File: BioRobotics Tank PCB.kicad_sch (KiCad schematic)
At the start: 35 parts, among them J1 Conn_01x02, J8 Conn_02x05_Odd_Even, J9 Conn_01x05, Q1 IPD060N03LGATMA1, U1 rp2040-zero, U6 TCA9554DB, U7 TCA9554DB, U8 LTC4357MS8, U9 INA219BIDR

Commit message: Add 10k pulldown to nSleep and export BOM
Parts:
- added R15: 10k, Resistor_SMD:R_0805_2012Metric_Pad1.20x1.40mm_HandSolder, symbol Device:R
- C3: Mfr. No (none) -> UVZ1J101MPD
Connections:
- net GND1: now also R15.2
- net ~{M_SLEEP}: now also R15.1
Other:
- note added: "Pulldown"
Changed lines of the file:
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@@
+    (stroke (width 0) (type default))
+  )
+  (wire (pts (xy 87.63 100.33) (xy 90.17 100.33))
     (stroke (width 0) (type default))
   )
@@
     (stroke (width 0) (type default))
   )
+  (wire (pts (xy 77.47 100.33) (xy 80.01 100.33))
+    (stroke (width 0) (type default))
+  )
   (wire (pts (xy 45.72 71.12) (xy 44.45 71.12))
     (stroke (width 0) (type default))
@@
     (stroke (width 0) (type default))
   )
+  (wire (pts (xy 90.17 101.6) (xy 90.17 100.33))
+    (stroke (width 0) (type default))
+  )
   (wire (pts (xy 149.86 86.36) (xy 151.13 86.36))
     (stroke (width 0) (type default))
@@
   )
   (rectangle (start 97.79 16.51) (end 160.02 71.12)
+    (stroke (width 0) (type default))
+    (fill (type none))
+  )
+  (rectangle (start 66.04 87.63) (end 95.25 110.49)
     (stroke (width 0) (type default))
     (fill (type none))
@@
     (effects (font (size 2.54 2.54) (thickness 0.508) bold) (justify left bottom))
   )
+  (text "Pulldown" (at 71.12 92.71 0)
+    (effects (font (size 2.54 2.54) (thickness 0.508) bold) (justify left bottom))
+  )
   (text "3.3V Regulator" (at 38.1 21.59 0)
     (effects (font (size 2.54 2.54) (thickness 0.508) bold) (justify left bottom))
@@
   )
   (label "GPIO11" (at 107.95 96.52 180) (fields_autoplaced)
+    (effects (font (size 1.27 1.27)) (justify right bottom))
+  )
+  (label "~{M_SLEEP}" (at 77.47 100.33 180) (fields_autoplaced)
     (effects (font (size 1.27 1.27)) (justify right bottom))
   )
@@
     )
   )
+  (symbol (lib_id "power:GND1") (at 90.17 101.6 0) (unit 1)
+    (in_bom yes) (on_board yes) (dnp no) (fields_autoplaced)
+    (property "Reference" "#PWR024" (at 90.17 107.95 0)
+      (effects (font (size 1.27 1.27)) hide)
+    )
+    (property "Value" "GND1" (at 90.17 106.68 0)
+      (effects (font (size 1.27 1.27)))
+    )
+    (property "Footprint" "" (at 90.17 101.6 0)
+      (effects (font (size 1.27 1.27)) hide)
+    )
+    (property "Datasheet" "" (at 90.17 101.6 0)
+      (effects (font (size 1.27 1.27)) hide)
+    )
+    (pin "1")
+    (instances
+      (project "BioRobotics Tank PCB"
+        (path "/738c766b-5149-4d22-8944-003aead1c6f2/91fbf09a-497d-4de7-ab4a-2985c5e3b4aa"
+          (reference "#PWR024") (unit 1)
+        )
+        (path "/738c766b-5149-4d22-8944-003aead1c6f2/a65e5353-4be6-414a-8225-04b1dd46f16e"
+          (reference "#PWR032") (unit 1)
+        )
+        (path "/738c766b-5149-4d22-8944-003aead1c6f2/917f7088-b2e9-4770-ad29-156eaf4e2242"
+          (reference "#PWR034") (unit 1)
+        )
+        (path "/738c766b-5149-4d22-8944-003aead1c6f2/05b32763-3ed9-4afa-8241-412ea6f0290d"
+          (reference "#PWR035") (unit 1)
+        )
+        (path "/738c766b-5149-4d22-8944-003aead1c6f2"
+          (reference "#PWR062") (unit 1)
+        )
+      )
+    )
+  )
   (symbol (lib_id "power:+3V3") (at 130.81 86.36 0) (unit 1)
     (in_bom yes) (on_board yes) (dnp no) (fields_autoplaced)
@@
     )
     (property "Datasheet" "~" (at 77.47 35.56 0)
+      (effects (font (size 1.27 1.27)) hide)
+    )
+    (property "Mfr. No" "UVZ1J101MPD" (at 77.47 35.56 0)
       (effects (font (size 1.27 1.27)) hide)
     )
@@
         )
       )
+    )
+  )
+  (symbol (lib_id "Device:R") (at 83.82 100.33 90) (unit 1)
+    (in_bom yes) (on_board yes) (dnp no) (fields_autoplaced)
+    (property "Reference" "R15" (at 83.82 95.25 90)
+      (effects (font (size 1.27 1.27)))
+    )
+    (property "Value" "10k" (at 83.82 97.79 90)
+      (effects (font (size 1.27 1.27)))
+    )
+    (property "Footprint" "Resistor_SMD:R_0805_2012Metric_Pad1.20x1.40mm_HandSolder" (at 83.82 102.108 90)
+      (effects (font (size 1.27 1.27)) hide)
+    )
+    (property "Datasheet" "~" (at 83.82 100.33 0)
+      (effects (font (size 1.27 1.27)) hide)
+    )
+    (property "Mfr. No" "CRS0805-FX-1002ELF" (at 83.82 100.33 90)
+      (effects (font (size 1.27 1.27)) hide)
+    )
+    (pin "1")
+    (pin "2")
+    (instances
+      (project "BioRobotics Tank PCB"
+        (path "/738c766b-5149-4d22-8944-003aead1c6f2"
+          (reference "R15") (unit 1)
+        )
+      )

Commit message: Update 0.1uF capacitor mfr no
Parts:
- C1: Mfr. No KGM21NR71E104KT -> 08055C104JAT2A
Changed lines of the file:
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@@
       (effects (font (size 1.27 1.27)) hide)
     )
-    (property "Mfr. No" "KGM21NR71E104KT" (at 26.67 39.37 90)
+    (property "Mfr. No" "08055C104JAT2A" (at 26.67 39.37 90)
       (effects (font (size 1.27 1.27)) hide)
     )
@@
       (effects (font (size 1.27 1.27)) hide)
     )
-    (property "Mfr. No" "KGM21NR71E104KT" (at 30.48 143.51 90)
+    (property "Mfr. No" "08055C104JAT2A" (at 30.48 143.51 90)
       (effects (font (size 1.27 1.27)) hide)
     )
@@
       (effects (font (size 1.27 1.27)) hide)
     )
-    (property "Mfr. No" "KGM21NR71E104KT" (at 53.34 95.25 90)
+    (property "Mfr. No" "08055C104JAT2A" (at 53.34 95.25 90)
       (effects (font (size 1.27 1.27)) hide)
     )
@@
       (effects (font (size 1.27 1.27)) hide)
     )
-    (property "Mfr. No" "KGM21NR71E104KT" (at 256.54 135.89 90)
+    (property "Mfr. No" "08055C104JAT2A" (at 256.54 135.89 90)
       (effects (font (size 1.27 1.27)) hide)
     )
@@
       (effects (font (size 1.27 1.27)) hide)
     )
-    (property "Mfr. No" "KGM21NR71E104KT" (at 93.98 140.97 90)
+    (property "Mfr. No" "08055C104JAT2A" (at 93.98 140.97 90)
       (effects (font (size 1.27 1.27)) hide)
     )
@@
       (effects (font (size 1.27 1.27)) hide)
     )
-    (property "Mfr. No" "KGM21NR71E104KT" (at 203.2 134.62 90)
+    (property "Mfr. No" "08055C104JAT2A" (at 203.2 134.62 90)
       (effects (font (size 1.27 1.27)) hide)
     )
@@
       (effects (font (size 1.27 1.27)) hide)
     )
-    (property "Mfr. No" "KGM21NR71E104KT" (at 82.55 35.56 90)
+    (property "Mfr. No" "08055C104JAT2A" (at 82.55 35.56 90)
       (effects (font (size 1.27 1.27)) hide)
     )
@@
       (effects (font (size 1.27 1.27)) hide)
     )
-    (property "Mfr. No" "KGM21NR71E104KT" (at 147.32 58.42 90)
-      (effects (font (size 1.27 1.27)) hide)
-    )
+    (property "Mfr. No" "08055C104JAT2A" (at 147.32 58.42 90)
+      (effects (font (size 1.27 1.27)) hide)
+    )

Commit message: Change Screw Terminal Part and update Mfr No's
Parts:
- J1: footprint TerminalBlock_Phoenix:TerminalBlock_Phoenix_MKDS-1,5-2-5.08_1x02_P5.08mm_Horizontal -> TB009-508-02BE:CUI_TB009-508-02BE; Mfr. No (none) -> TB009-508-02BE
- J8: Mfr. No (none) -> 61201021621
- PS1: Mfr. No (none) -> P78E03-1000
- Q1: Mfr. No (none) -> IPD060N03LGATMA1
- U8: Mfr. No (none) -> LTC4357CMS8#PBF
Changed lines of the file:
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@@
       (effects (font (size 1.27 1.27)) (justify left))
     )
-    (property "Footprint" "TerminalBlock_Phoenix:TerminalBlock_Phoenix_MKDS-1,5-2-5.08_1x02_P5.08mm_Horizontal" (at 123.19 127 0)
+    (property "Footprint" "TB009-508-02BE:CUI_TB009-508-02BE" (at 123.19 127 0)
       (effects (font (size 1.27 1.27)) hide)
     )
     (property "Datasheet" "~" (at 123.19 127 0)
+      (effects (font (size 1.27 1.27)) hide)
+    )
+    (property "Mfr. No" "TB009-508-02BE" (at 123.19 127 0)
       (effects (font (size 1.27 1.27)) hide)
     )
@@
       (effects (font (size 1.27 1.27)) (justify left bottom) hide)
     )
+    (property "Mfr. No" "P78E03-1000" (at 49.53 35.56 0)
+      (effects (font (size 1.27 1.27)) hide)
+    )
     (pin "1")
     (pin "2")
@@
     (property "Arrow Price/Stock" "https://www.arrow.com/en/products/ipd060n03lgatma1/infineon-technologies-ag?region=nac" (at -964.44 67.31 0)
       (effects (font (size 1.27 1.27)) (justify left top) hide)
+    )
+    (property "Mfr. No" "IPD060N03LGATMA1" (at 34.29 78.74 90)
+      (effects (font (size 1.27 1.27)) hide)
     )
     (pin "1")
@@
       (effects (font (size 1.27 1.27)) hide)
     )
+    (property "Mfr. No" "61201021621" (at 116.84 93.98 0)
+      (effects (font (size 1.27 1.27)) hide)
+    )
     (pin "1")
     (pin "10")
@@
       (effects (font (size 1.27 1.27)) hide)
     )
+    (property "Mfr. No" "LTC4357CMS8#PBF" (at 43.18 88.9 0)
+      (effects (font (size 1.27 1.27)) hide)
+    )
     (pin "1")
     (pin "2")
@@
       (effects (font (size 1.27 1.27)) (justify left))
     )
-    (property "Footprint" "TerminalBlock_Phoenix:TerminalBlock_Phoenix_MKDS-1,5-2-5.08_1x02_P5.08mm_Horizontal" (at 123.19 139.7 0)
+    (property "Footprint" "TB009-508-02BE:CUI_TB009-508-02BE" (at 123.19 139.7 0)
       (effects (font (size 1.27 1.27)) hide)
     )
     (property "Datasheet" "~" (at 123.19 139.7 0)
+      (effects (font (size 1.27 1.27)) hide)
+    )
+    (property "Mfr. No" "TB009-508-02BE" (at 123.19 139.7 0)
       (effects (font (size 1.27 1.27)) hide)
     )
@@
       (effects (font (size 1.27 1.27)) (justify left))
     )
-    (property "Footprint" "TerminalBlock_Phoenix:TerminalBlock_Phoenix_MKDS-1,5-2-5.08_1x02_P5.08mm_Horizontal" (at 123.19 133.35 0)
+    (property "Footprint" "TB009-508-02BE:CUI_TB009-508-02BE" (at 123.19 133.35 0)
       (effects (font (size 1.27 1.27)) hide)
     )
@@
       (effects (font (size 1.27 1.27)) hide)
     )
+    (property "Mfr. No" "TB009-508-02BE" (at 123.19 133.35 0)
+      (effects (font (size 1.27 1.27)) hide)
+    )

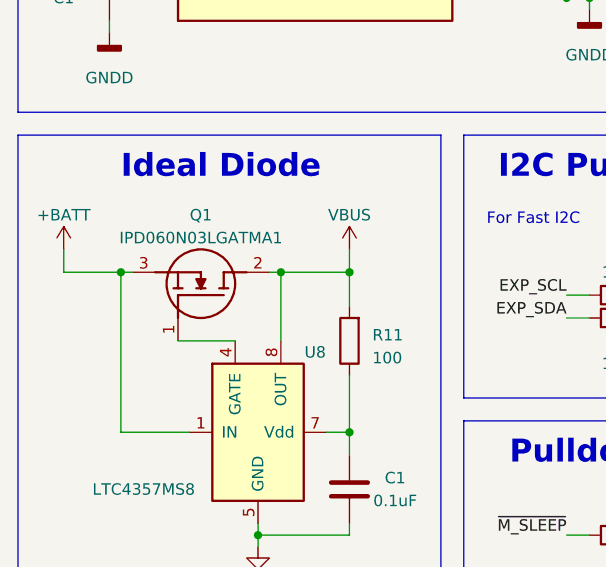
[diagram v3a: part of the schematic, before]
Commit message: Change ideal diode mosfet and increase track sizes
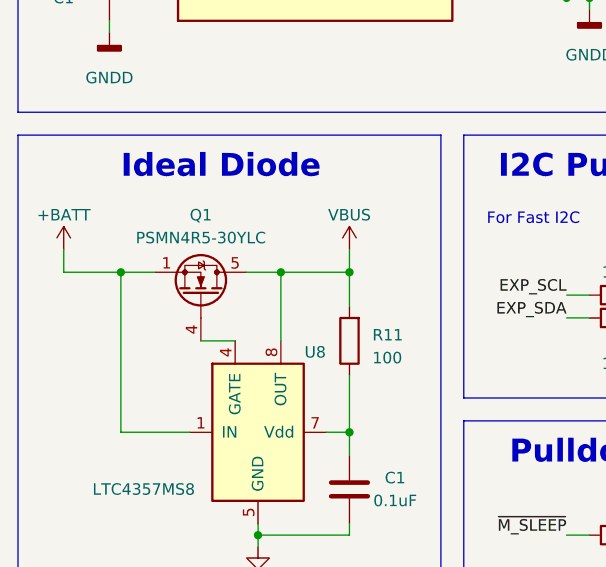
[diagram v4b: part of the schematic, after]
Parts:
- removed Q1: IPD060N03LGATMA1, IPD060N03LGATMA1:IPD060N03LGATMA1, symbol IPD060N03LGATMA1:IPD060N03LGATMA1
- added Q1: PSMN4R5-30YLC, Package_TO_SOT_SMD:LFPAK56, symbol Transistor_FET:PSMN5R2-60YL
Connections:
- net +BATT: now also Q1.1 (S), Q1.2 (S), Q1.3 (S)
- net VBUS: now also Q1.5 (D)
- net at U8.4 (GATE): now also Q1.4 (G)
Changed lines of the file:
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@@
-    (stroke (width 0) (type default))
-  )
-  (wire (pts (xy 34.29 78.74) (xy 40.64 78.74))
     (stroke (width 0) (type default))
   )
@@
     (stroke (width 0) (type default))
   )
-  (wire (pts (xy 27.94 71.12) (xy 29.21 71.12))
+  (wire (pts (xy 27.94 71.12) (xy 31.75 71.12))
     (stroke (width 0) (type default))
   )
@@
     (stroke (width 0) (type default))
   )
-  (wire (pts (xy 45.72 71.12) (xy 44.45 71.12))
+  (wire (pts (xy 41.91 71.12) (xy 45.72 71.12))
     (stroke (width 0) (type default))
   )
@@
   )
   (wire (pts (xy 82.55 31.75) (xy 82.55 30.48))
+    (stroke (width 0) (type default))
+  )
+  (wire (pts (xy 36.83 78.74) (xy 40.64 78.74))
     (stroke (width 0) (type default))
   )
@@
         (path "/738c766b-5149-4d22-8944-003aead1c6f2"
           (reference "JP2") (unit 1)
-        )
-      )
-    )
-  )
-  (symbol (lib_id "IPD060N03LGATMA1:IPD060N03LGATMA1") (at 34.29 78.74 270) (mirror x) (unit 1)
-    (in_bom yes) (on_board yes) (dnp no)
-    (property "Reference" "Q1" (at 36.83 64.77 90)
-      (effects (font (size 1.27 1.27)))
-    )
-    (property "Value" "IPD060N03LGATMA1" (at 36.83 67.31 90)
-      (effects (font (size 1.27 1.27)))
-    )
-    (property "Footprint" "IPD060N03LGATMA1:IPD060N03LGATMA1" (at -64.44 67.31 0)
-      (effects (font (size 1.27 1.27)) (justify left top) hide)
-    )
-    (property "Datasheet" "https://www.infineon.com/dgdl/Infineon-IPD060N03L%20G-DataSheet-v02_02-EN.pdf?fileId=db3a30432313ff5e01239e4d33a3702f" (at -164.44 67.31 0)
-      (effects (font (size 1.27 1.27)) (justify left top) hide)
-    )
-    (property "Height" "2.5" (at -364.44 67.31 0)
-      (effects (font (size 1.27 1.27)) (justify left top) hide)
-    )
-    (property "Manufacturer_Name" "Infineon" (at -464.44 67.31 0)
-      (effects (font (size 1.27 1.27)) (justify left top) hide)
-    )
-    (property "Manufacturer_Part_Number" "IPD060N03LGATMA1" (at -564.44 67.31 0)
-      (effects (font (size 1.27 1.27)) (justify left top) hide)
-    )
-    (property "Mouser Part Number" "726-IPD060N03LGATMA1" (at -664.44 67.31 0)
-      (effects (font (size 1.27 1.27)) (justify left top) hide)
-    )
-    (property "Mouser Price/Stock" "https://www.mouser.co.uk/ProductDetail/Infineon-Technologies/IPD060N03LGATMA1?qs=Dj8dEyEphkPMHEbgPBJgAQ%3D%3D" (at -764.44 67.31 0)
-      (effects (font (size 1.27 1.27)) (justify left top) hide)
-    )
-    (property "Arrow Part Number" "IPD060N03LGATMA1" (at -864.44 67.31 0)
-      (effects (font (size 1.27 1.27)) (justify left top) hide)
-    )
-    (property "Arrow Price/Stock" "https://www.arrow.com/en/products/ipd060n03lgatma1/infineon-technologies-ag?region=nac" (at -964.44 67.31 0)
-      (effects (font (size 1.27 1.27)) (justify left top) hide)
-    )
-    (property "Mfr. No" "IPD060N03LGATMA1" (at 34.29 78.74 90)
-      (effects (font (size 1.27 1.27)) hide)
-    )
-    (pin "1")
-    (pin "2")
-    (pin "3")
-    (instances
-      (project "BioRobotics Tank PCB"
-        (path "/738c766b-5149-4d22-8944-003aead1c6f2"
-          (reference "Q1") (unit 1)
         )
       )
@@
         )
       )
+    )
+  )
+  (symbol (lib_id "Transistor_FET:PSMN5R2-60YL") (at 36.83 73.66 270) (mirror x) (unit 1)
+    (in_bom yes) (on_board yes) (dnp no)
+    (property "Reference" "Q1" (at 36.83 64.77 90)
+      (effects (font (size 1.27 1.27)))
+    )
+    (property "Value" "PSMN4R5-30YLC" (at 36.83 67.31 90)
+      (effects (font (size 1.27 1.27)))
+    )
+    (property "Footprint" "Package_TO_SOT_SMD:LFPAK56" (at 36.83 69.85 0)
+      (effects (font (size 1.27 1.27)) hide)
+    )
+    (property "Datasheet" "https://www.mouser.co.uk/datasheet/2/916/PSMN4R5_30YLC-2938954.pdf" (at 36.83 73.66 0)
+      (effects (font (size 1.27 1.27)) hide)
+    )
+    (property "Mfr. No" "PSMN4R5-30YLC,115" (at 36.83 73.66 90)
+      (effects (font (size 1.27 1.27)) hide)
+    )
+    (pin "1")
+    (pin "2")
+    (pin "3")
+    (pin "4")
+    (pin "5")
+    (instances
+      (project "BioRobotics Tank PCB"
+        (path "/738c766b-5149-4d22-8944-003aead1c6f2"
+          (reference "Q1") (unit 1)
+        )
+      )
